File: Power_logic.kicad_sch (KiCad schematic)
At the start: 6 parts

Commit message: Power changes
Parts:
- removed Bat_3.3V_direct1, Bat_5V_direct1, Plug_3.3V_direct1, USB_5V_direct1, Vref_3.3V_CM41, Vref_3.3V_STM1: DNP, Resistor_SMD:R_0603_1608Metric, symbol #dzdb:g_res/R-0-0603
- added R34, R35, R36, R37, R38, R41, R42, R43, R44, R45, R46, R47: 0, Resistor_SMD:R_0603_1608Metric, symbol #dzdb:g_res/R-0-0603
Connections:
- net Battery_Out_3.3V: now also R44.1, R47.1
- net Battery_Out_5V: now also R35.1, R36.1
- net CM4_LED_IN_3.3V: now also R38.1, R43.1
- net GPIO_VREF_3.3V: now also R38.2, R41.2
- net STM_Plug_3.3V: now also R45.1, R46.1
- net USB_Out_5V: now also R34.1, R37.1
- new net +3.3V: R41.1, R42.1, R46.2, R47.2
- new net +5V: R34.2, R35.2
- new net 3.3V_Logic/Battery_Out_3.3V: R44.2
- new net 3.3V_Logic/STM_Plug_3.3V: R45.2
- new net 5V_Logic/Battery_Out_5V: R36.2
- new net 5V_Logic/USB_Out_5V: R37.2
- new net GPIO_REF3.3V/CM4_OUT_3.3V: R43.2
- new net GPIO_REF3.3V/STM_IN_3.3V: R42.2
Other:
- note added: "Directly connected if plug is in"
- note added: "place to activate"
- note added: "place to deactivate"
- note removed: "If STM has power, power the gyro and accelerometer"
- note removed: "LED APHHS1005LSECK/J3-PF"
- note removed: "R 1.6k"
- note removed: "Wont work... diodes are not perfect..."
- note removed: "if there is a battery connected, the LED will light up and you should not plug in your USB cable/STM connector."
- note removed: "maybe scrap this?"

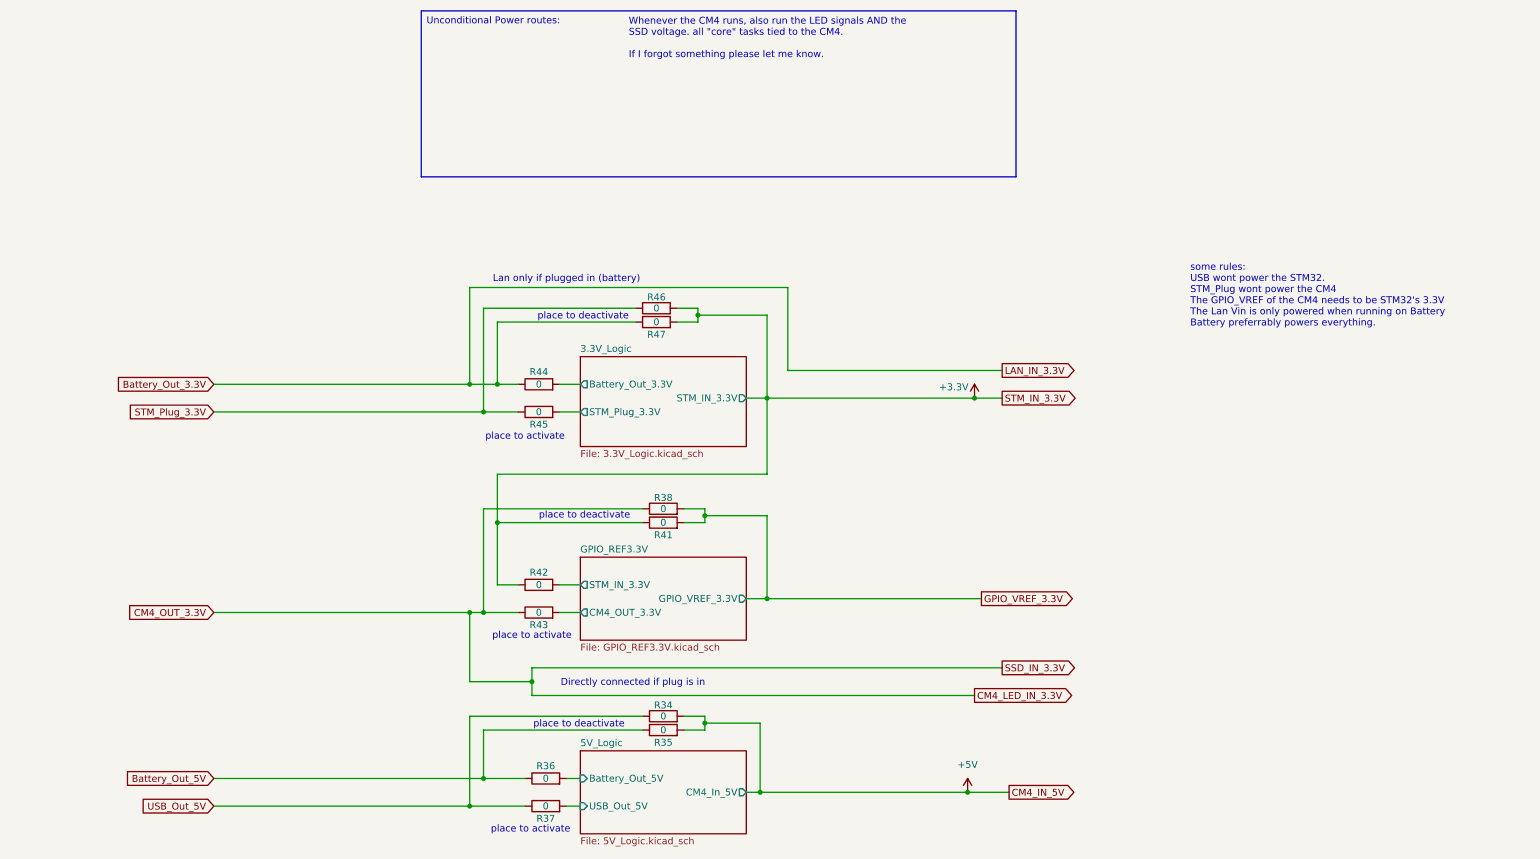
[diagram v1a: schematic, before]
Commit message: chore: multiple cosmetic wiring changes
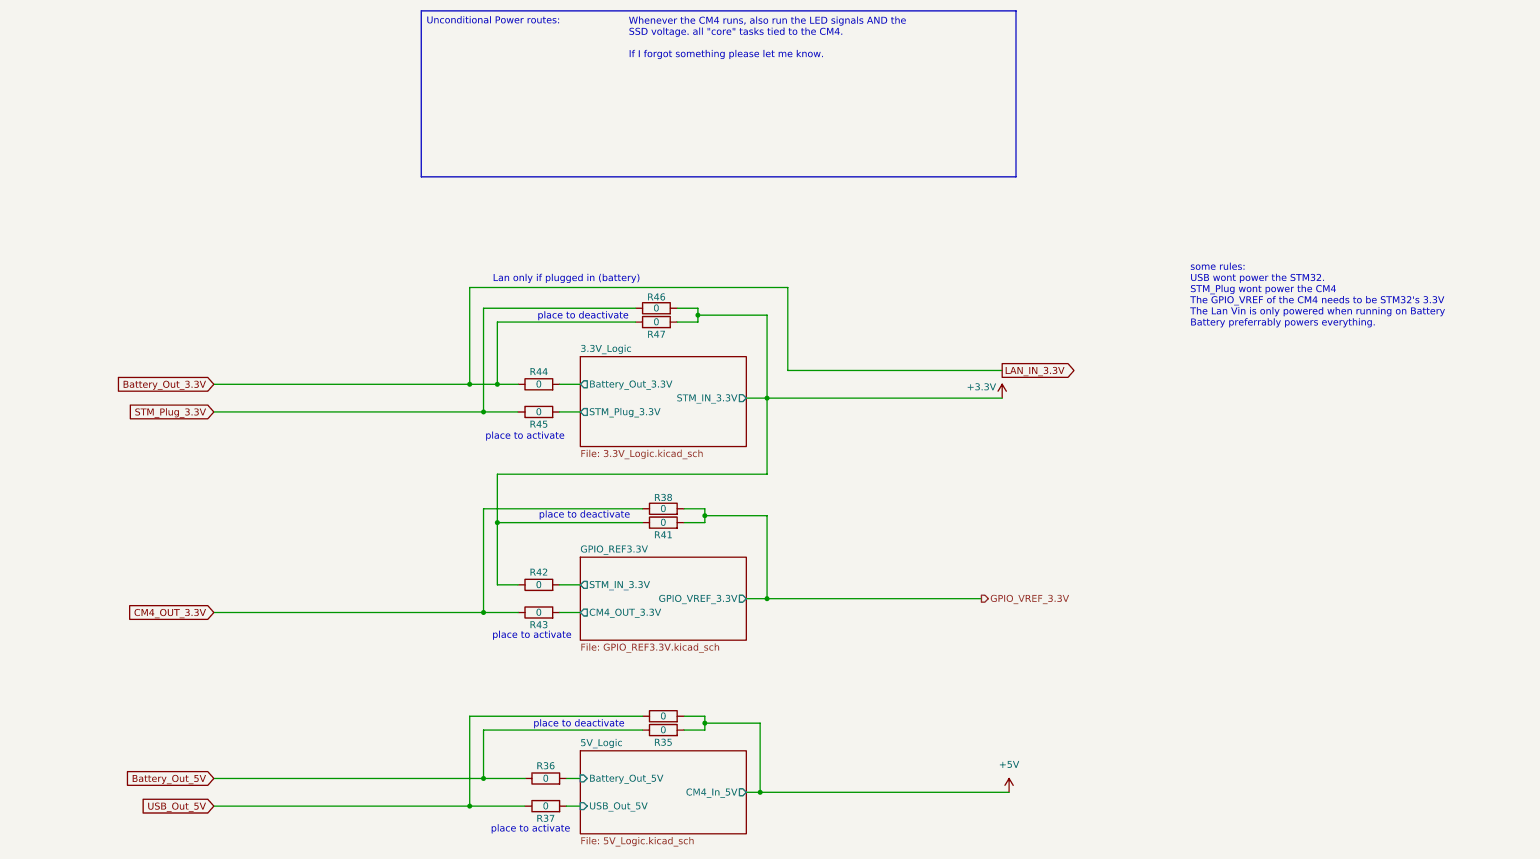
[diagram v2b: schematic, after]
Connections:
- net CM4_LED_IN_3.3V renamed CM4_OUT_3.3V
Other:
- note removed: "Directly connected if plug is in"

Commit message: chore: Many routing changes
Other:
- note added: "Different Power Sources."
- note added: "Reference power sources"
- note added: "Whenever the CM4 runs, also run the LED signals AND the SSD voltage. all "core" tasks tied to the CM4."
- note removed: "Whenever the CM4 runs, also run the LED signals AND the SSD voltage. all "core" tasks tied to the CM4. If I forgot something please let me know."
- company: (none) -> dcarocci

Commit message: chore: more cleanup
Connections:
- net CM4_OUT_3.3V is gone; now on net CM4_Out_3.3V: R38.1, R43.1
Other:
- sheet 3.3V_Logic ports: added STM_In_3.3V; removed STM_IN_3.3V
- company: dcarocci -> Davide
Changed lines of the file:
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@@
 	(title_block
 		(date "2025-11-18")
-		(company "dcarocci")
+		(company "Davide")
 	)
 	(text "place to activate"
@@
 		)
 	)
-	(global_label "CM4_OUT_3.3V"
-		(shape input)
-		(at 73.66 127 180)
-		(fields_autoplaced yes)
-		(effects
-			(font
-				(size 1.27 1.27)
-			)
-			(justify right)
-		)
-		(property "Intersheetrefs" "${INTERSHEET_REFS}"
-			(at 57.0677 127 0)
-			(effects
-				(font
-					(size 1.27 1.27)
-				)
-				(justify right)
-				(hide yes)
-			)
-		)
-	)
 	(hierarchical_label "STM_Plug_3.3V"
 		(shape input)
@@
 	(hierarchical_label "CM4_Out_3.3V"
 		(shape input)
-		(at 73.66 124.46 180)
+		(at 73.66 127 180)
 		(effects
 			(font
@@
 			)
 		)
-		(pin "Battery_Out_3.3V" output
+		(pin "Battery_Out_3.3V" input
 			(at 119.38 85.09 180)
 			(effects
@@
 			)
 		)
-		(pin "STM_IN_3.3V" output
-			(at 149.86 87.63 0)
+		(pin "STM_Plug_3.3V" input
+			(at 119.38 90.17 180)
 			(effects
 				(font
 					(size 1.27 1.27)
 				)
-				(justify right)
+				(justify left)
 			)
 		)
-		(pin "STM_Plug_3.3V" output
-			(at 119.38 90.17 180)
+		(pin "STM_In_3.3V" output
+			(at 149.86 87.63 0)
 			(effects
 				(font
 					(size 1.27 1.27)
 				)
-				(justify left)
+				(justify right)
 			)
 		)
@@
 			)
 		)
-		(pin "CM4_OUT_3.3V" output
-			(at 119.38 127 180)
+		(pin "GPIO_VREF_3.3V" output
+			(at 149.86 124.46 0)
 			(effects
 				(font
 					(size 1.27 1.27)
 				)
-				(justify left)
+				(justify right)
 			)
 		)
-		(pin "GPIO_VREF_3.3V" output
-			(at 149.86 124.46 0)
+		(pin "STM_IN_3.3V" input
+			(at 119.38 121.92 180)
 			(effects
 				(font
 					(size 1.27 1.27)
 				)
-				(justify right)
+				(justify left)
 			)
 		)
-		(pin "STM_IN_3.3V" output
-			(at 119.38 121.92 180)
+		(pin "CM4_OUT_3.3V" input
+			(at 119.38 127 180)
 			(effects
 				(font

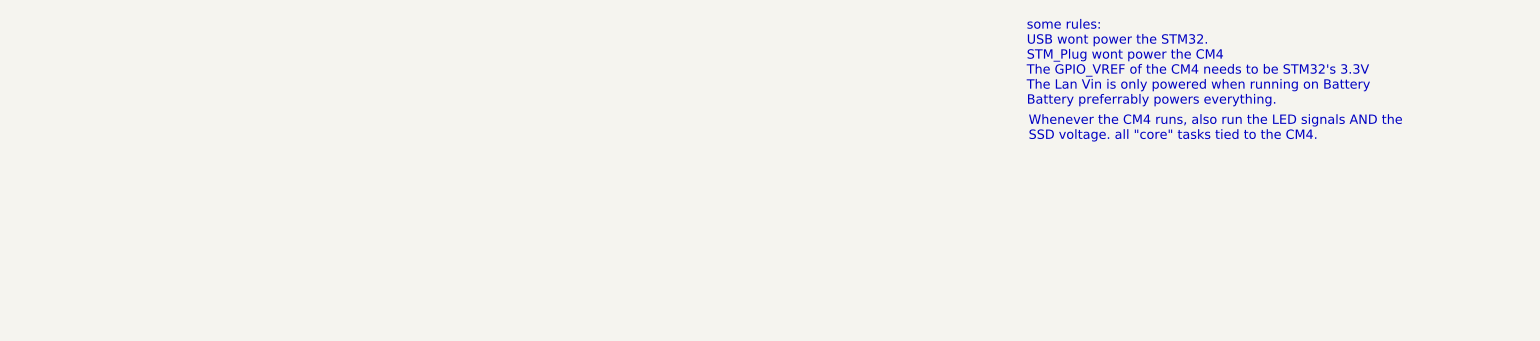
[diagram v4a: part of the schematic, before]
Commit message: chore: added LED indicators for power and activity status, updated symbold, rerouted some things for better visibility
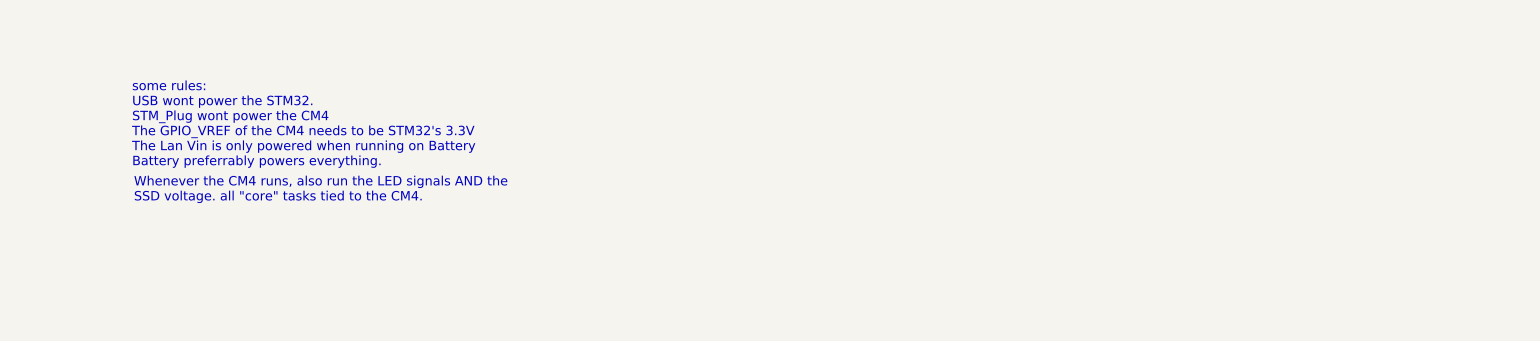
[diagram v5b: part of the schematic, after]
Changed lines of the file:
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@@
 	(paper "A4")
 	(title_block
-		(date "2025-11-18")
+		(date "2025-11-19")
+		(rev "1")
 		(company "Davide")
 	)
@@
 	(text "Whenever the CM4 runs, also run the LED signals AND the\nSSD voltage. all \"core\" tasks tied to the CM4."
 		(exclude_from_sim no)
-		(at 223.52 33.528 0)
+		(at 101.6 41.91 0)
 		(effects
 			(font
@@
 	(text "some rules:\nUSB wont power the STM32.\nSTM_Plug wont power the CM4\nThe GPIO_VREF of the CM4 needs to be STM32's 3.3V\nThe Lan Vin is only powered when running on Battery\nBattery preferrably powers everything."
 		(exclude_from_sim no)
-		(at 223.266 24.638 0)
+		(at 101.346 33.02 0)
 		(effects
 			(font

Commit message: chore: Loads of redoing stuff. Added a Changelog
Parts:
- added LED10, LED9: 710-150060RS83000, dz_dio:Wuerth_LED_150060RS83000, symbol #dzdb:s_dio/D-WURT-710-150060RS83000
- added R24, R25: 1k, Resistor_SMD:R_0603_1608Metric, symbol #dzdb:g_res/R-1k-0603
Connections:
- net +3.3V: now also R24.2
- net +5V: now also R25.2
- new net: LED10.2 (A), R25.1
- new net: LED9.2 (A), R24.1
- new net GND: LED10.1 (K), LED9.1 (K)
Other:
- note added: "I_{F} = 20mA V_{in} = 3.3V V_{F} ≈ 2.0V"
- note added: "I_{F} = 20mA V_{in} = 5V V_{F} ≈ 2.0V"
- note added: "R= (V_{in} - V_{F}) / I_{F}"
- note added: "So min R is 150Ω"
- note added: "So min R is 68Ω"
- title: (none) -> Nautilus_Mainboard

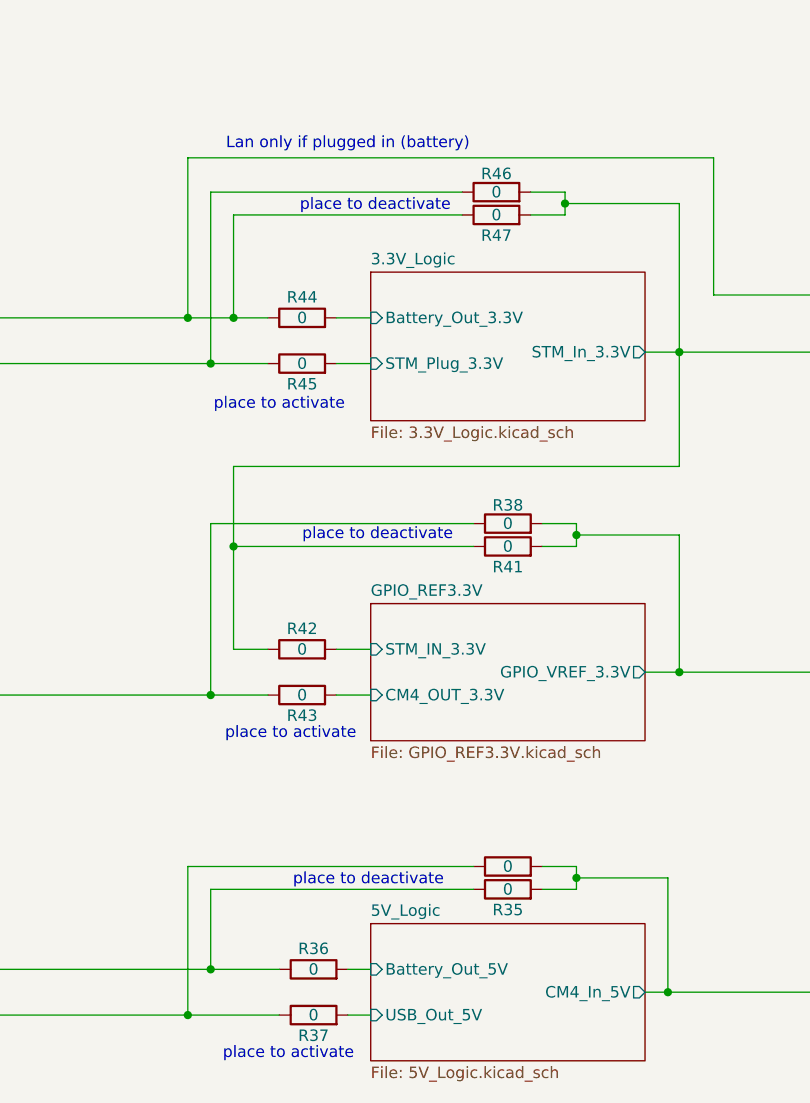
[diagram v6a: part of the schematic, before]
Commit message: chore: replaced 0 ohm with jumpers (not complete)
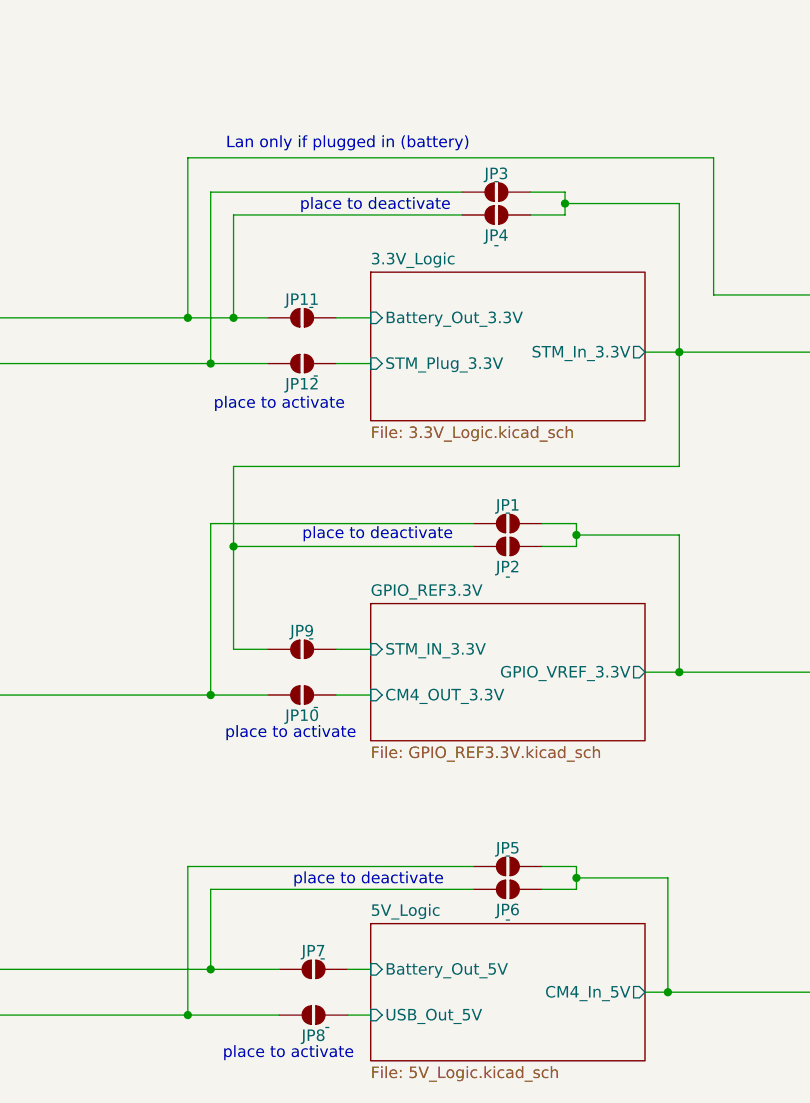
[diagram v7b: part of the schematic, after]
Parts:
- removed R34, R35, R36, R37, R38, R41, R42, R43, R44, R45, R46, R47: 0, Resistor_SMD:R_0603_1608Metric, symbol #dzdb:g_res/R-0-0603
- added JP1, JP10, JP11, JP12, JP2, JP3, JP4, JP5, JP6, JP7, JP8, JP9: -, Jumper:SolderJumper-2_P1.3mm_Open_RoundedPad1.0x1.5mm, symbol #dzdb:g_mech/Jumper-2P1.3mm_Rounded
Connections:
- net +3.3V: now also JP2.1 (A), JP3.2 (B), JP4.2 (B), JP9.1 (A)
- net +5V: now also JP5.2 (B), JP6.2 (B)
- net 3.3V_Logic/Battery_Out_3.3V: now also JP11.2 (B)
- net 3.3V_Logic/STM_Plug_3.3V: now also JP12.2 (B)
- net 5V_Logic/Battery_Out_5V: now also JP7.2 (B)
- net 5V_Logic/USB_Out_5V: now also JP8.2 (B)
- net Battery_Out_3.3V: now also JP11.1 (A), JP4.1 (A)
- net Battery_Out_5V: now also JP6.1 (A), JP7.1 (A)
- net CM4_Out_3.3V: now also JP1.1 (A), JP10.1 (A)
- net GPIO_REF3.3V/CM4_OUT_3.3V: now also JP10.2 (B)
- net GPIO_REF3.3V/STM_IN_3.3V: now also JP9.2 (B)
- net GPIO_VREF_3.3V: now also JP1.2 (B), JP2.2 (B)
- net STM_Plug_3.3V: now also JP12.1 (A), JP3.1 (A)
- net USB_Out_5V: now also JP5.1 (A), JP8.1 (A)

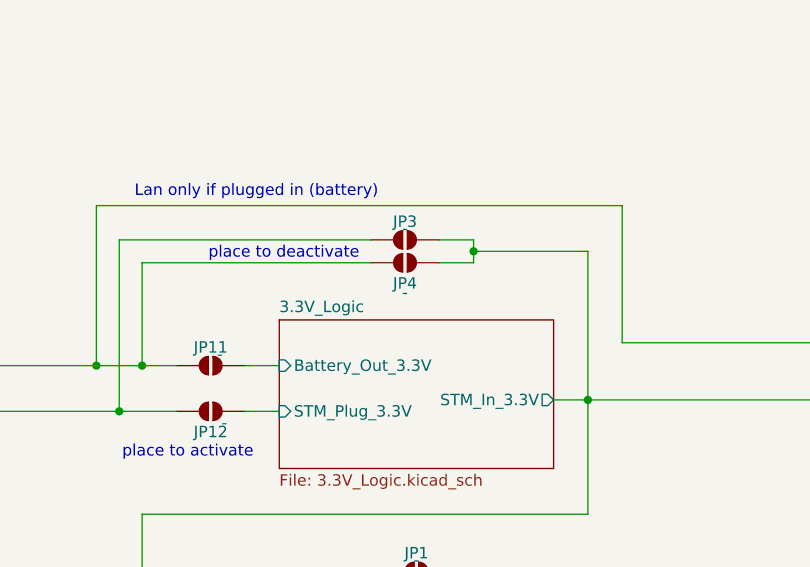
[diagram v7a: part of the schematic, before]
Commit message: chore: routed the Jumpers (incomplete) fix: removed all leftover 0Ohm resistors
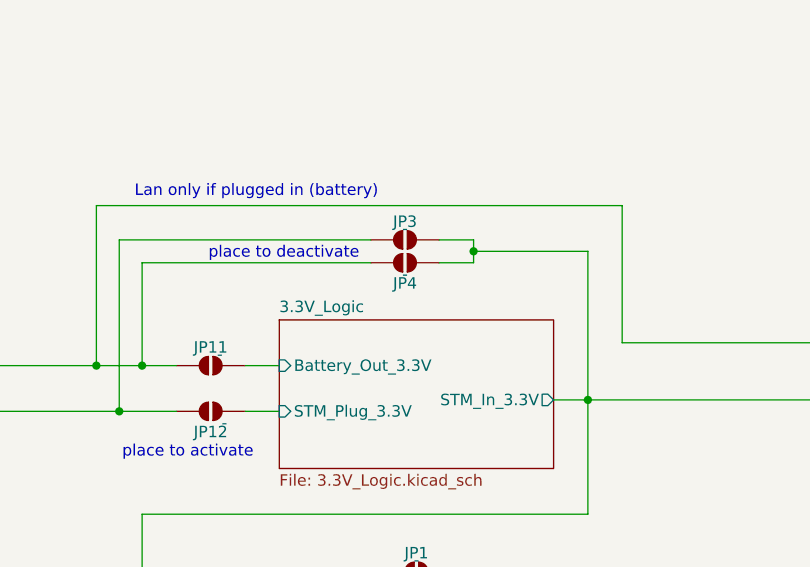
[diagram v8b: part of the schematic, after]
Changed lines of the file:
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@@
 		)
 		(property "Value" "-"
-			(at 133.35 76.962 0)
+			(at 133.35 69.85 0)
 			(effects
 				(font
@@
 		)
 		(property "Value" "-"
-			(at 133.35 69.85 0)
-			(effects
-				(font
+			(at 133.35 74.93 0)
+			(effects
+				(font
